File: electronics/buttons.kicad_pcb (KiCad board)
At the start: 2 copper layers, 60 x 21 mm, 11 parts, among them J1 Conn_01x02, J2 Conn_01x02, J3 Conn_01x02, J4 Conn_01x02, SW1 SW_Push, SW2 SW_Push, SW3 SW_Push, SW4 SW_Push

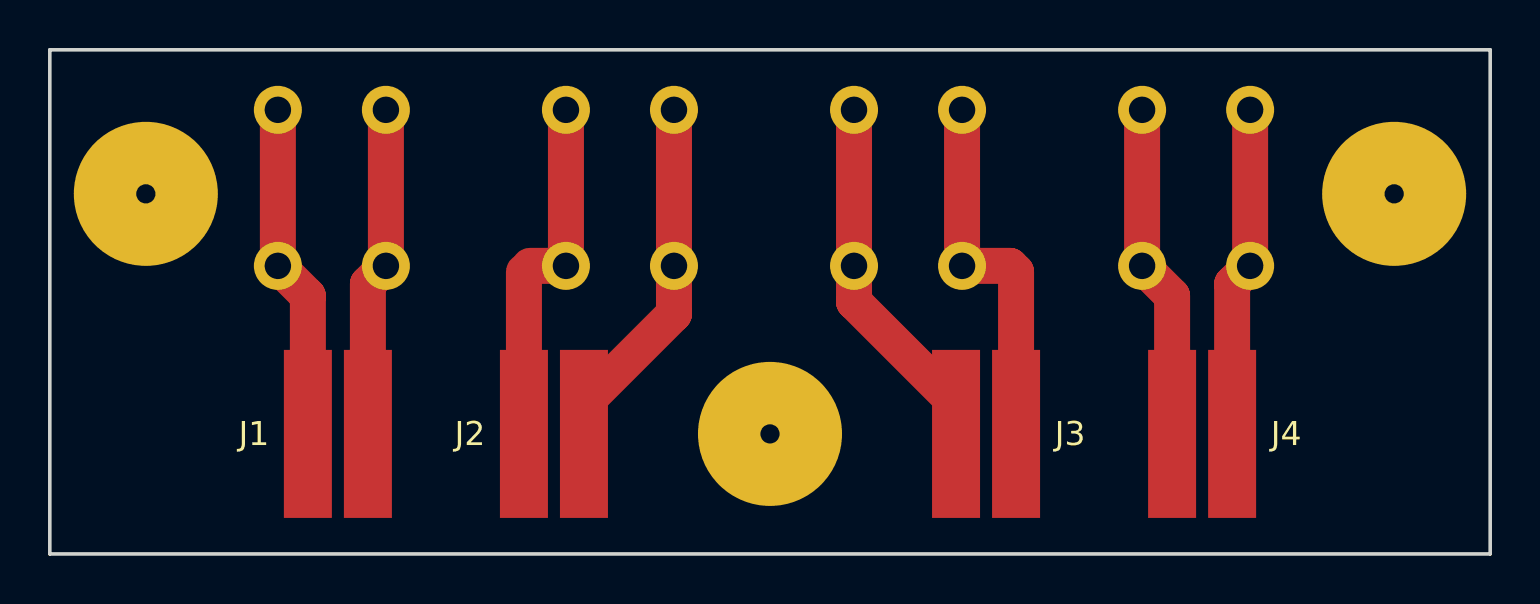
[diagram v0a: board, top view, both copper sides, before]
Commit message: Schematic of ring for lambda/4
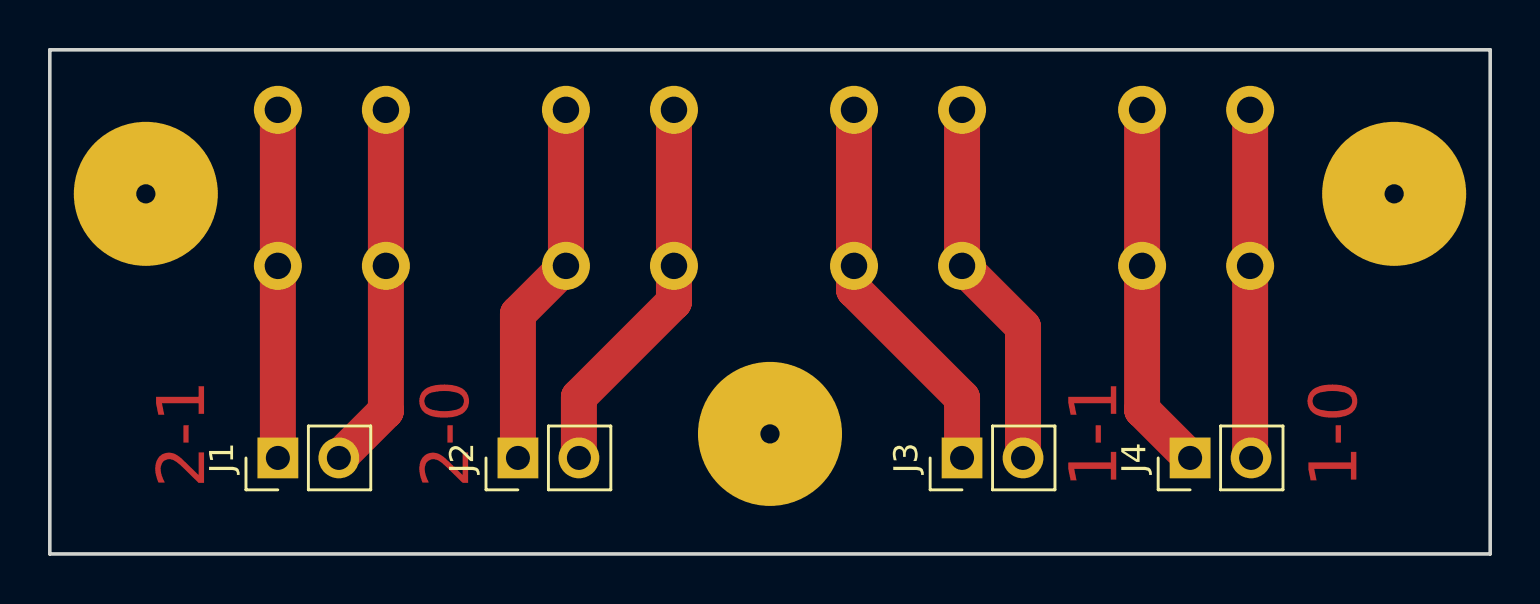
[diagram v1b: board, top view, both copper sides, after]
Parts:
- J1, J2, J3, J4: footprint my_footprints:SMD2pin -> Pin_Headers.pretty:Pin_Header_Straight_1x02_Pitch2.54mm
- moved J1 2.69 mm to (98.5, 87.0), turned to 90 degrees
- moved J2 1.80 mm to (108.5, 87.0), turned to 90 degrees
- moved J3 1.41 mm to (127.0, 87.0), turned to 90 degrees
- moved J4 1.12 mm to (136.5, 87.0), turned to 90 degrees
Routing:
- net Net-(J1-Pad2): track 13.8 -> 15.3 mm
- net Net-(J4-Pad1): track 14.0 -> 15.3 mm
- net Net-(J3-Pad1): track 15.3 -> 16.4 mm
- net Net-(J2-Pad2): track 15.1 -> 16.1 mm
- net Net-(J4-Pad2): track 13.8 -> 14.5 mm
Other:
- board text added: "1-0"
- board text added: "1-1"
- board text added: "2-0"
- board text added: "2-1"
